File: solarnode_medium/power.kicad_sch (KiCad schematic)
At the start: 22 parts, among them J1 Conn_01x06, U1 YX59012, U2 SGM2033-3.3, U7 YX59012

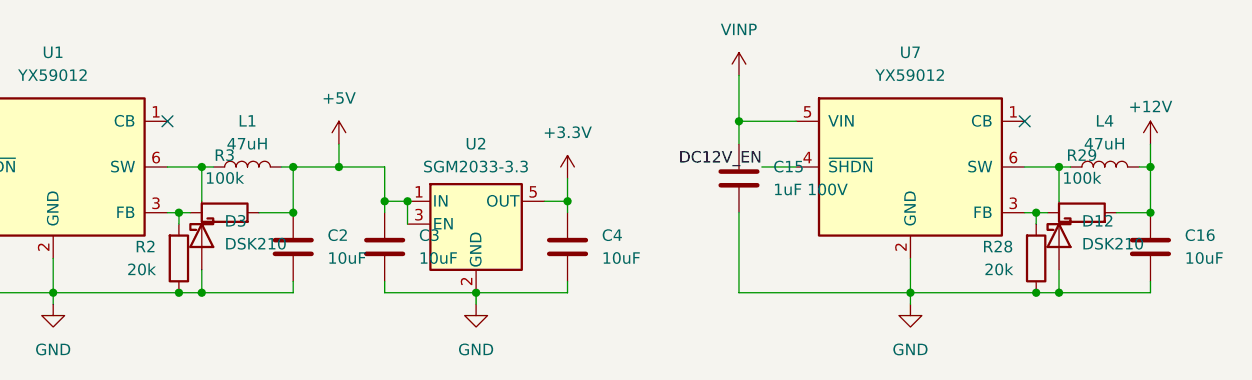
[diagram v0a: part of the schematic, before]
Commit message: PCB元器件分组和局部布局
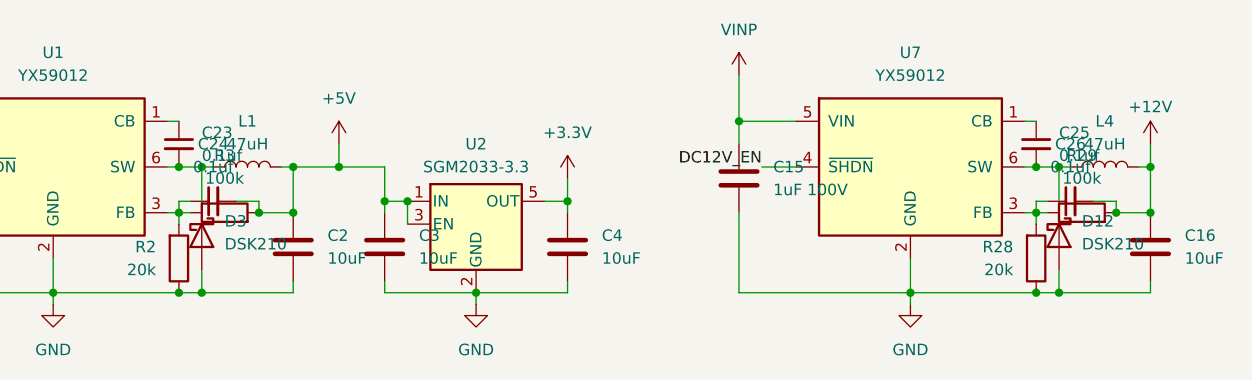
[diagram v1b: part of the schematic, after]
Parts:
- added C23, C24, C25, C26: 0.1uf, Capacitor_SMD:C_0402_1005Metric, symbol Device:C_Small
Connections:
- net +12V: now also C26.2
- net +5V: now also C24.2
- net at R2.2, R3.1, U1.3 (FB): now also C24.1
- net at D12.1 (K), L4.1, U7.6 (SW): now also C25.2
- net at U7.1 (CB): now also C25.1
- net at R28.2, R29.1, U7.3 (FB): now also C26.1
- net at U1.1 (CB): now also C23.1
- net at D3.1 (K), L1.1, U1.6 (SW): now also C23.2
- no-connect marks 2 -> 0

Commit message: 修改原理图，添加子原理图间连接，添加MCU和一些外围电路
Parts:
- removed D1, D2: DSF1D, Diode_SMD:D_SOD-123F, symbol Device:D
- removed F3: 2A, Fuse:Fuse_1206_3216Metric, symbol Device:Fuse
- removed J1: Conn_01x06, TerminalBlock:TerminalBlock_bornier-6_P5.08mm, symbol Connector_Generic:Conn_01x06

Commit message: 添加备用电池充电和电源切换电路
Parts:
- added BT1: Battery_Cell, Connector_PinSocket_2.54mm:PinSocket_1x02_P2.54mm_Vertical, symbol Device:Battery_Cell
- added C36, C37: 1uf, Capacitor_SMD:C_0603_1608Metric, symbol Device:C
- added C38: C, Capacitor_SMD:C_0603_1608Metric, symbol Device:C
- added D15, D16: LED, LED_SMD:LED_0603_1608Metric, symbol Device:LED
- added D17: D_Schottky, Diode_SMD:D_SOD-123F, symbol Device:D_Schottky
- added Q9: PMOS, Package_TO_SOT_SMD:SOT-23, symbol Simulation_SPICE:PMOS
- added R31: 0.4, Resistor_SMD:R_1206_3216Metric, symbol Device:R
- added R43: 330, Resistor_SMD:R_0603_1608Metric, symbol Device:R
- added R44: R, Resistor_SMD:R_0402_1005Metric, symbol Device:R
- added R45, R46: R, Capacitor_SMD:C_0402_1005Metric, symbol Device:R
- added R47: 100k, Capacitor_SMD:C_0402_1005Metric, symbol Device:R
- added R48: 1k, Capacitor_SMD:C_0402_1005Metric, symbol Device:R
- added U9: CN3058E, Package_SO:HTSOP-8-1EP_3.9x4.9mm_P1.27mm_EP2.4x3.2mm, symbol New_Library:CN3058E
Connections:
- net +5V: now also D17.2 (A), R31.1, R43.1, R48.1; no longer C3.1, U2.1 (IN), U2.3 (EN)
- net GND: now also BT1.2 (-), C36.2, C37.2, C38.2, R44.2, R46.2, R47.1, U9.3 (GND), U9.9 (EP)
- new net: Q9.2 (G), R47.2, R48.2
- new net: R45.2, R46.1, U9.1 (TEMP)
- new net: D15.2 (A), D16.2 (A), R43.2
- new net: R44.1, U9.2 (ISET)
- new net: BT1.1 (+), C37.1, Q9.1 (D), U9.5 (BAT), U9.8 (FB)
- new net: C36.1, R31.2, R45.1, U9.4 (VIN)
- new net: D16.1 (K), U9.6 (~{DONE})
- new net: D15.1 (K), U9.7 (~{CHRG})
- new net +5VB: C3.1, C38.1, D17.1 (K), Q9.3 (S), U2.1 (IN), U2.3 (EN)
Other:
- note added: "使用一节磷酸铁锂电池"
